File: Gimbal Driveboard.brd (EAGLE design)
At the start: 68.1 x 82.9 mm, 26 parts, among them J2 APP_2POS_CONFIG12V_HORIZ, U1 OKI-78SR-5/1.5-W36HC, U2 MAX232D, U3 MAX232D

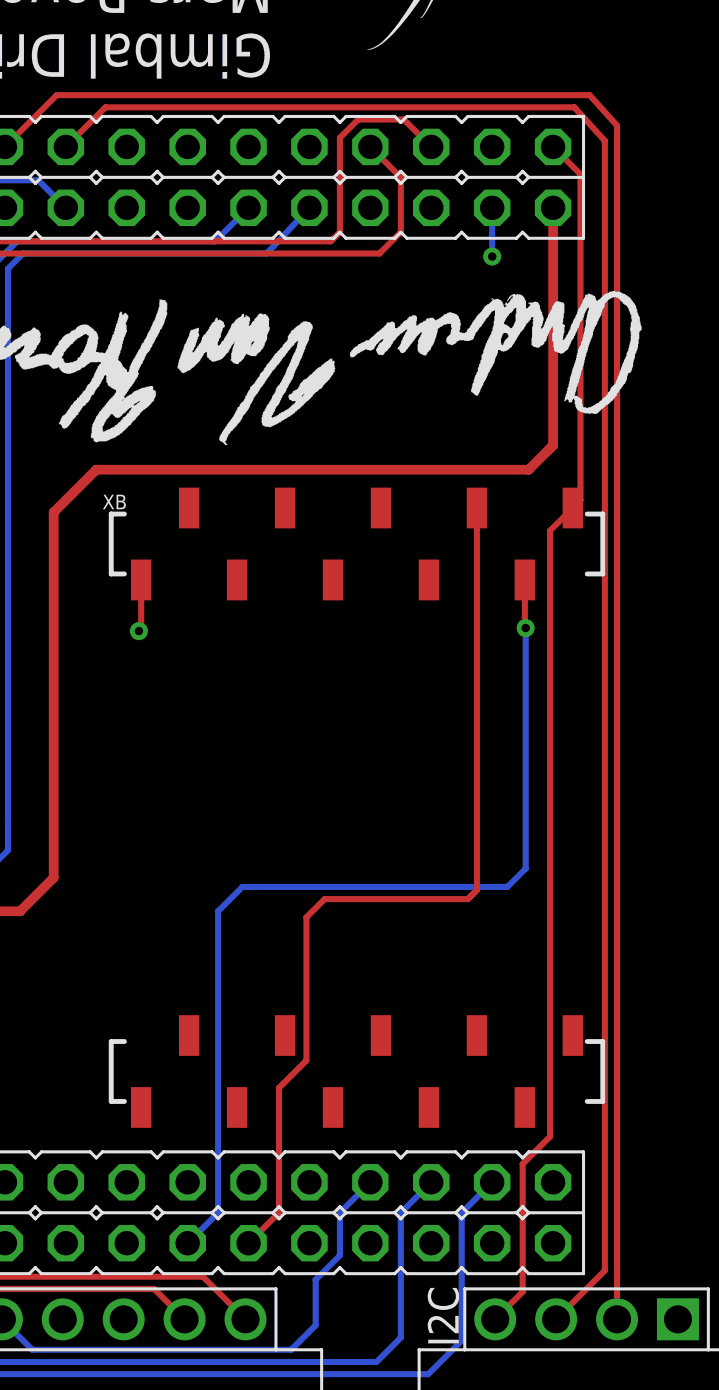
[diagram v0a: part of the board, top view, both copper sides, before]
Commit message: Re-routed XB Serial to Serial 2
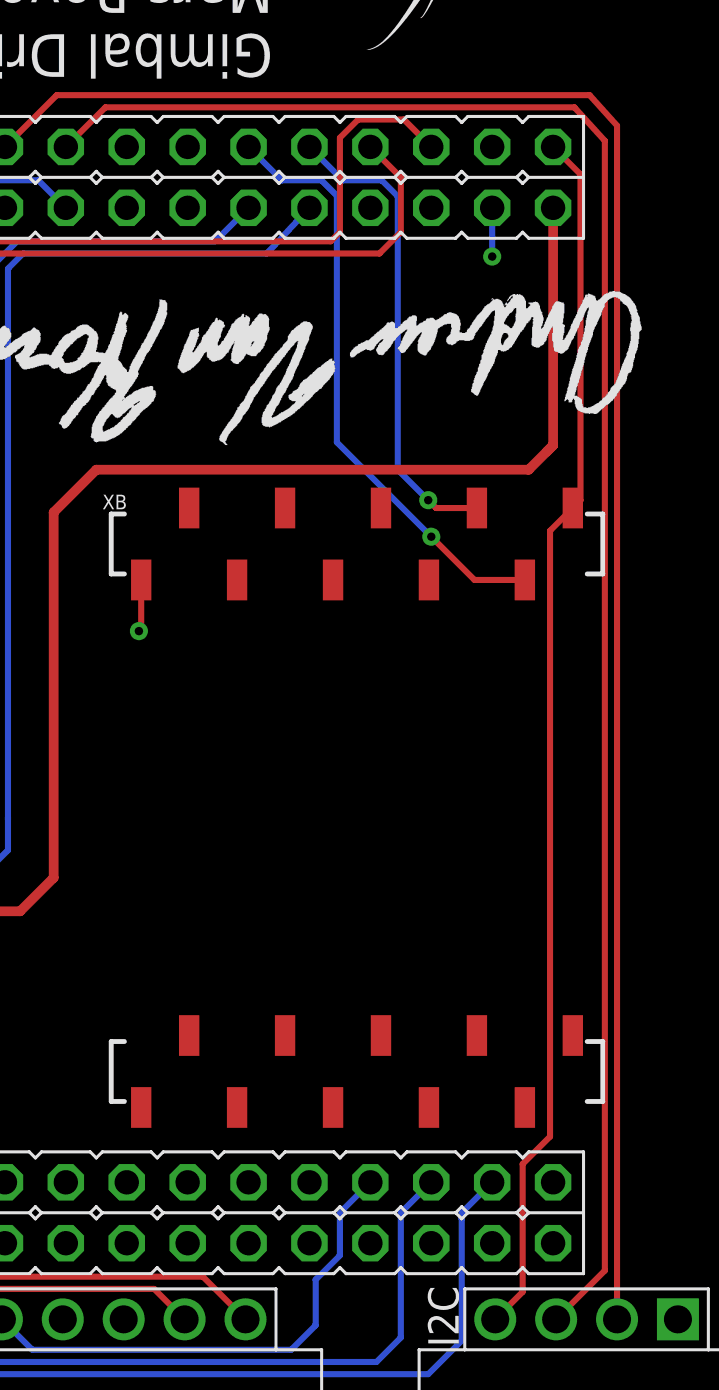
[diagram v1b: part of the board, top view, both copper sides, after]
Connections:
- net XB_RX: now also U$2.5; no longer U$2.34
- net XB_TX: now also U$2.6; no longer U$2.35
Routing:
- net XB_TX: track 38.5 -> 19.9 mm, vias 0 -> 1
- net XB_RX: track 40.1 -> 25.0 mm
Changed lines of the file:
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@@
 <signal name="XB_RX">
 <contactref element="XB" pad="2"/>
-<wire x1="59.021" y1="38.329" x2="59.021" y2="36.356" width="0.254" layer="1"/>
-<wire x1="59.021" y1="36.356" x2="59.055" y2="36.322" width="0.254" layer="1"/>
-<via x="59.055" y="36.322" extent="1-16" drill="0.35"/>
-<wire x1="59.055" y1="36.322" x2="59.055" y2="26.289" width="0.254" layer="16"/>
-<wire x1="59.055" y1="26.289" x2="58.293" y2="25.527" width="0.254" layer="16"/>
-<wire x1="58.293" y1="25.527" x2="47.244" y2="25.527" width="0.254" layer="16"/>
-<wire x1="46.228" y1="24.511" x2="46.228" y2="11.811" width="0.254" layer="16"/>
-<wire x1="47.244" y1="25.527" x2="46.228" y2="24.511" width="0.254" layer="16"/>
-<contactref element="U$2" pad="34"/>
-<wire x1="46.228" y1="11.811" x2="46.101" y2="11.811" width="0.254" layer="16"/>
-<wire x1="46.101" y1="11.811" x2="44.958" y2="10.668" width="0.254" layer="16"/>
+<contactref element="U$2" pad="5"/>
+<wire x1="47.498" y1="56.388" x2="48.895" y2="54.991" width="0.254" layer="16"/>
+<wire x1="48.895" y1="54.991" x2="50.546" y2="54.991" width="0.254" layer="16"/>
+<wire x1="50.546" y1="54.991" x2="51.181" y2="54.356" width="0.254" layer="16"/>
+<wire x1="51.181" y1="44.069" x2="55.118" y2="40.132" width="0.254" layer="16"/>
+<via x="55.118" y="40.132" extent="1-16" drill="0.35"/>
+<wire x1="51.181" y1="54.356" x2="51.181" y2="44.069" width="0.254" layer="16"/>
+<wire x1="55.118" y1="40.132" x2="56.921" y2="38.329" width="0.254" layer="1"/>
+<wire x1="56.921" y1="38.329" x2="59.021" y2="38.329" width="0.254" layer="1"/>
 </signal>
 <signal name="XB_TX">
 <contactref element="XB" pad="3"/>
-<wire x1="57.021" y1="41.329" x2="57.021" y2="25.398" width="0.254" layer="1"/>
-<wire x1="56.896" y1="25.273" x2="57.021" y2="25.398" width="0.254" layer="1"/>
-<wire x1="56.896" y1="25.273" x2="56.642" y2="25.019" width="0.254" layer="1"/>
-<wire x1="48.768" y1="17.145" x2="48.768" y2="11.811" width="0.254" layer="1"/>
-<wire x1="48.768" y1="17.145" x2="49.911" y2="18.288" width="0.254" layer="1"/>
-<wire x1="49.911" y1="18.288" x2="49.911" y2="24.257" width="0.254" layer="1"/>
-<wire x1="49.911" y1="24.257" x2="50.673" y2="25.019" width="0.254" layer="1"/>
-<wire x1="50.673" y1="25.019" x2="56.642" y2="25.019" width="0.254" layer="1"/>
-<wire x1="56.642" y1="25.019" x2="56.896" y2="25.273" width="0.254" layer="1"/>
-<contactref element="U$2" pad="35"/>
-<wire x1="48.768" y1="11.811" x2="48.641" y2="11.811" width="0.254" layer="1"/>
-<wire x1="48.641" y1="11.811" x2="47.498" y2="10.668" width="0.254" layer="1"/>
+<contactref element="U$2" pad="6"/>
+<wire x1="53.05145" y1="54.991" x2="53.721" y2="54.32145" width="0.254" layer="16"/>
+<wire x1="50.038" y1="56.388" x2="51.435" y2="54.991" width="0.254" layer="16"/>
+<wire x1="51.435" y1="54.991" x2="53.05145" y2="54.991" width="0.254" layer="16"/>
+<wire x1="53.721" y1="42.926" x2="54.991" y2="41.656" width="0.254" layer="16"/>
+<wire x1="53.721" y1="54.32145" x2="53.721" y2="42.926" width="0.254" layer="16"/>
+<via x="54.991" y="41.656" extent="1-16" drill="0.35"/>
+<wire x1="54.991" y1="41.656" x2="55.318" y2="41.329" width="0.254" layer="1"/>
+<wire x1="55.318" y1="41.329" x2="57.021" y2="41.329" width="0.254" layer="1"/>
 </signal>
 <signal name="SDA">
